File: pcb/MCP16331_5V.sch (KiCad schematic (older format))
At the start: 13 parts, among them U8 MCP16331T

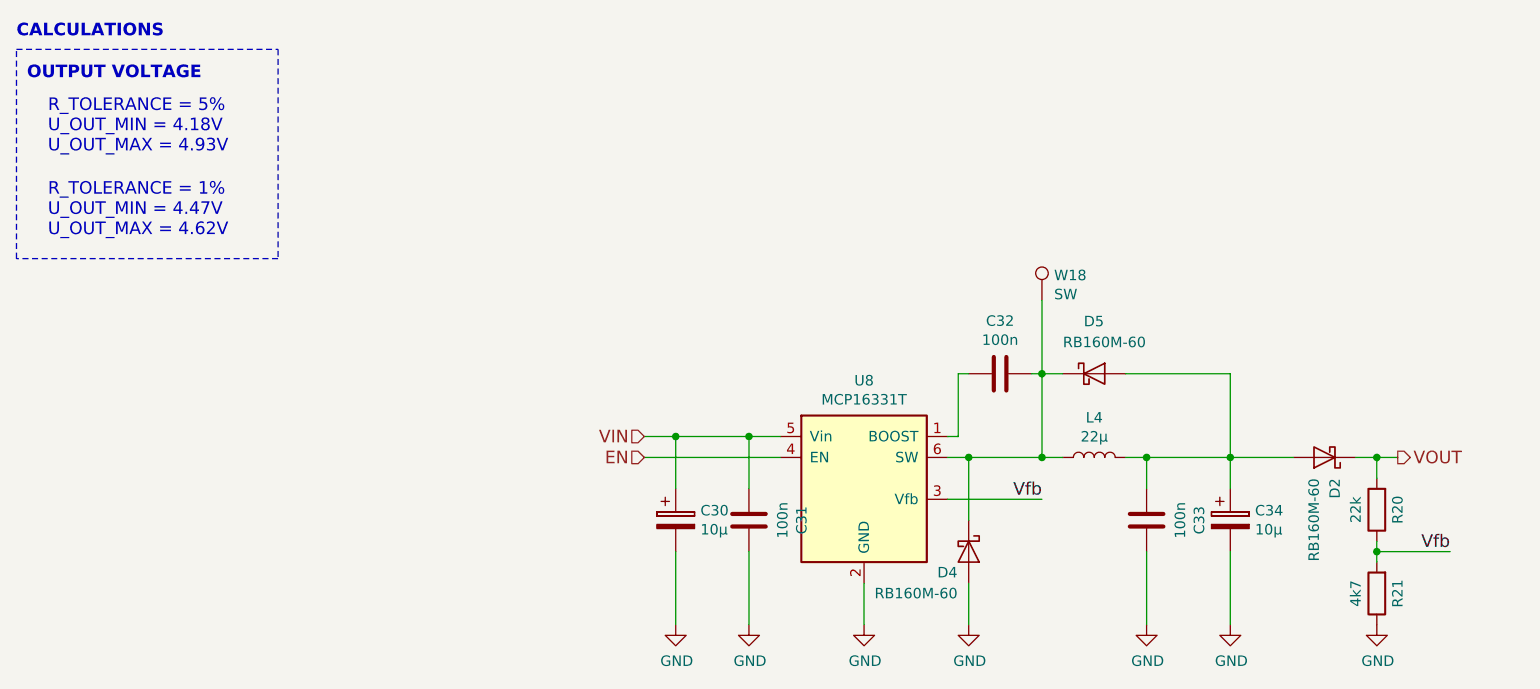
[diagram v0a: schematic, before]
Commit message: Fix schematic error described in #8
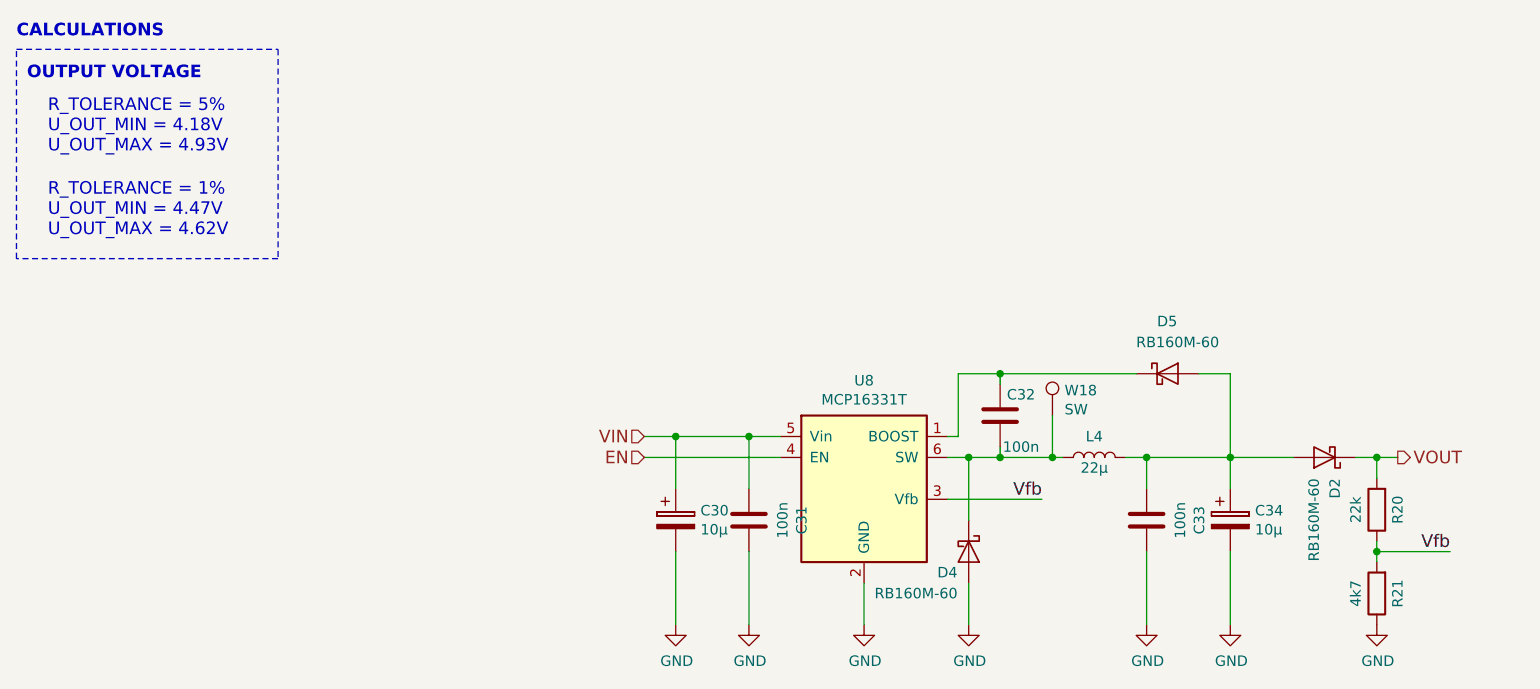
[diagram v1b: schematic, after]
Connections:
- net at C32.1, U8.1 (BOOST): now also D5.1 (K)
- net at C32.2, D4.1 (K), L4.1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: no longer D5.1 (K)
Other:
- moved on the sheet: C32, D5, W18
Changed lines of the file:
@@
 $EndComp
 $Comp
-L GND #PWR095
+L GND #PWR094
 U 1 1 580BA37A
 P 5300 4250
-F 0 "#PWR095" H 5300 4000 50  0001 C CNN
+F 0 "#PWR094" H 5300 4000 50  0001 C CNN
 F 1 "GND" H 5305 4077 50  0000 C CNN
 F 2 "" H 5300 4250 50  0000 C CNN
@@
 $EndComp
 $Comp
-L GND #PWR096
+L GND #PWR095
 U 1 1 580BA3A1
 P 4750 4250
-F 0 "#PWR096" H 4750 4000 50  0001 C CNN
+F 0 "#PWR095" H 4750 4000 50  0001 C CNN
 F 1 "GND" H 4755 4077 50  0000 C CNN
 F 2 "" H 4750 4250 50  0000 C CNN
@@
 $EndComp
 $Comp
-L GND #PWR097
+L GND #PWR096
 U 1 1 580BA3A7
 P 4400 4250
-F 0 "#PWR097" H 4400 4000 50  0001 C CNN
+F 0 "#PWR096" H 4400 4000 50  0001 C CNN
 F 1 "GND" H 4405 4077 50  0000 C CNN
 F 2 "" H 4400 4250 50  0000 C CNN
@@
 Wire Wire Line
 	4400 3900 4400 4250
-$Comp
-L C C32
-U 1 1 580BA3AF
-P 5950 3050
-F 0 "C32" V 6202 3050 50  0000 C CNN
-F 1 "100n" V 6111 3050 50  0000 C CNN
-F 2 "Capacitors_SMD:C_0603" H 5988 2900 50  0001 C CNN
-F 3 "" H 5950 3050 50  0000 C CNN
-F 4 "311-1343-1-ND" H 5950 3050 60  0001 C CNN "Digi-Key Part Number"
-F 5 "1" H 5950 3050 60  0001 C CNN "Digi-Key Minimum Quantity"
-	1    5950 3050
-	0    -1   -1   0
-$EndComp
-Wire Wire Line
-	5700 3450 6250 3450
-Wire Wire Line
-	6100 3050 6250 3050
-Wire Wire Line
-	6150 2700 6150 3450
-Connection ~ 6150 3450
+Wire Wire Line
+	5700 3450 5800 3450
+Wire Wire Line
+	5800 3450 5950 3450
+Wire Wire Line
+	5950 3450 6200 3450
+Wire Wire Line
+	6200 3450 6250 3450
 Wire Wire Line
 	5700 3350 5750 3350
 Wire Wire Line
-	5750 3350 5750 3050
-Wire Wire Line
-	5750 3050 5800 3050
+	5750 3050 5950 3050
+Wire Wire Line
+	5950 3050 6600 3050
 $Comp
 L CP C34
@@
 $EndComp
 $Comp
-L GND #PWR098
+L GND #PWR097
 U 1 1 580BA3CF
 P 6650 4250
-F 0 "#PWR098" H 6650 4000 50  0001 C CNN
+F 0 "#PWR097" H 6650 4000 50  0001 C CNN
 F 1 "GND" H 6655 4077 50  0000 C CNN
 F 2 "" H 6650 4250 50  0000 C CNN
@@
 $EndComp
 $Comp
-L GND #PWR099
+L GND #PWR098
 U 1 1 580BA3D5
 P 7050 4250
-F 0 "#PWR099" H 7050 4000 50  0001 C CNN
+F 0 "#PWR098" H 7050 4000 50  0001 C CNN
 F 1 "GND" H 7055 4077 50  0000 C CNN
 F 2 "" H 7050 4250 50  0000 C CNN
@@
 $EndComp
 $Comp
-L GND #PWR0100
+L GND #PWR099
 U 1 1 580BA3EB
 P 7750 4250
-F 0 "#PWR0100" H 7750 4000 50  0001 C CNN
+F 0 "#PWR099" H 7750 4000 50  0001 C CNN
 F 1 "GND" H 7755 4077 50  0000 C CNN
 F 2 "" H 7750 4250 50  0000 C CNN
@@
 Connection ~ 5800 3450
 $Comp
-L GND #PWR0101
+L GND #PWR0100
 U 1 1 580BA3FF
 P 5800 4250
-F 0 "#PWR0101" H 5800 4000 50  0001 C CNN
+F 0 "#PWR0100" H 5800 4000 50  0001 C CNN
 F 1 "GND" H 5805 4077 50  0000 C CNN
 F 2 "" H 5800 4250 50  0000 C CNN
@@
 L D_Schottky D5
 U 1 1 580BA407
-P 6400 3050
-F 0 "D5" H 6350 3300 50  0000 L CNN
-F 1 "RB160M-60" H 6250 3200 50  0000 L CNN
-F 2 "Diodes_SMD:SOD-123" H 6400 3050 50  0001 C CNN
-F 3 "" H 6400 3050 50  0000 C CNN
-	1    6400 3050
-	1    0    0    -1
-$EndComp
-Connection ~ 6150 3050
-Wire Wire Line
-	6550 3050 7050 3050
-Wire Wire Line
-	7050 3050 7050 3600
-Wire Wire Line
-	6550 3450 7350 3450
+P 6750 3050
+F 0 "D5" H 6700 3300 50  0000 L CNN
+F 1 "RB160M-60" H 6600 3200 50  0000 L CNN
+F 2 "Diodes_SMD:SOD-123" H 6750 3050 50  0001 C CNN
+F 3 "" H 6750 3050 50  0000 C CNN
+	1    6750 3050
+	1    0    0    -1
+$EndComp
+Wire Wire Line
+	6900 3050 7050 3050
+Wire Wire Line
+	7050 3050 7050 3450
+Wire Wire Line
+	7050 3450 7050 3600
+Wire Wire Line
+	6550 3450 6650 3450
+Wire Wire Line
+	6650 3450 7050 3450
+Wire Wire Line
+	7050 3450 7350 3450
 Wire Wire Line
 	6650 3450 6650 3600
@@
 VOUT
 Wire Wire Line
-	4250 3350 4900 3350
+	4250 3350 4400 3350
+Wire Wire Line
+	4400 3350 4750 3350
+Wire Wire Line
+	4750 3350 4900 3350
 Wire Wire Line
 	4400 3350 4400 3600
@@
 L TEST_1P W18
 U 1 1 5817A2DF
-P 6150 2700
-F 0 "W18" H 6208 2820 50  0000 L CNN
-F 1 "SW" H 6208 2729 50  0000 L CNN
-F 2 "Measurement_Points:Measurement_Point_Round-SMD-Pad_Small" H 6350 2700 50  0001 C CNN
-F 3 "" H 6350 2700 50  0000 C CNN
-	1    6150 2700
+P 6200 3250
+F 0 "W18" H 6258 3370 50  0000 L CNN
+F 1 "SW" H 6258 3279 50  0000 L CNN
+F 2 "Measurement_Points:Measurement_Point_Round-SMD-Pad_Small" H 6400 3250 50  0001 C CNN
+F 3 "" H 6400 3250 50  0000 C CNN
+	1    6200 3250
 	1    0    0    -1
 $EndComp
@@
 U 1 1 582ECCE6
 P 6400 3450
-F 0 "L4" V 6590 3450 50  0000 C CNN
-F 1 "22µ" V 6499 3450 50  0000 C CNN
+F 0 "L4" V 6500 3450 50  0000 C CNN
+F 1 "22µ" V 6350 3450 50  0000 C CNN
 F 2 "Inductors_local:Inductor_Würth_WE-PD2_4532" V 6498 3450 50  0001 C CNN
 F 3 "http://katalog.we-online.de/pbs/datasheet/744773122.pdf" V 6498 3450 50  0001 C CNN
@@
 $EndComp
 Wire Wire Line
-	7850 3450 7650 3450
+	7650 3450 7750 3450
+Wire Wire Line
+	7750 3450 7850 3450
 Wire Wire Line
 	7750 3550 7750 3450
 Connection ~ 7750 3450
 Wire Wire Line
-	7750 3850 7750 3950
+	7750 3850 7750 3900
+Wire Wire Line
+	7750 3900 7750 3950
 Wire Wire Line
 	7750 3900 8100 3900
@@
 Wire Wire Line
 	4750 3600 4750 3350
+$Comp
+L C C32
+U 1 1 580BA3AF
+P 5950 3250
+F 0 "C32" H 6050 3350 50  0000 C CNN
+F 1 "100n" H 6050 3100 50  0000 C CNN
+F 2 "Capacitors_SMD:C_0603" H 5988 3100 50  0001 C CNN
+F 3 "" H 5950 3250 50  0000 C CNN
+F 4 "311-1343-1-ND" H 5950 3250 60  0001 C CNN "Digi-Key Part Number"
+F 5 "1" H 5950 3250 60  0001 C CNN "Digi-Key Minimum Quantity"
+	1    5950 3250
+	1    0    0    -1
+$EndComp
+Wire Wire Line
+	5750 3350 5750 3050
+Wire Wire Line
+	5950 3450 5950 3400
+Connection ~ 5950 3450
+Wire Wire Line
+	5950 3100 5950 3050
+Connection ~ 5950 3050
+Wire Wire Line
+	6200 3250 6200 3450
+Connection ~ 6200 3450
 $EndSCHEMATC

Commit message: Update schematic
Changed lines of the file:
@@
 	4400 3900 4400 4250
 Wire Wire Line
-	5700 3450 5800 3450
-Wire Wire Line
-	5800 3450 5950 3450
-Wire Wire Line
-	5950 3450 6200 3450
-Wire Wire Line
-	6200 3450 6250 3450
+	5700 3450 6250 3450
 Wire Wire Line
 	5700 3350 5750 3350
 Wire Wire Line
-	5750 3050 5950 3050
-Wire Wire Line
-	5950 3050 6600 3050
+	5750 3050 6600 3050
 $Comp
 L CP C34
@@
 	6900 3050 7050 3050
 Wire Wire Line
-	7050 3050 7050 3450
-Wire Wire Line
-	7050 3450 7050 3600
-Wire Wire Line
-	6550 3450 6650 3450
-Wire Wire Line
-	6650 3450 7050 3450
-Wire Wire Line
-	7050 3450 7350 3450
+	7050 3050 7050 3600
+Wire Wire Line
+	6550 3450 7350 3450
 Wire Wire Line
 	6650 3450 6650 3600
@@
 VOUT
 Wire Wire Line
-	4250 3350 4400 3350
-Wire Wire Line
-	4400 3350 4750 3350
-Wire Wire Line
-	4750 3350 4900 3350
+	4250 3350 4900 3350
 Wire Wire Line
 	4400 3350 4400 3600
@@
 $EndComp
 Wire Wire Line
-	7650 3450 7750 3450
-Wire Wire Line
-	7750 3450 7850 3450
+	7650 3450 7850 3450
 Wire Wire Line
 	7750 3550 7750 3450
 Connection ~ 7750 3450
 Wire Wire Line
-	7750 3850 7750 3900
-Wire Wire Line
-	7750 3900 7750 3950
+	7750 3850 7750 3950
 Wire Wire Line
 	7750 3900 8100 3900

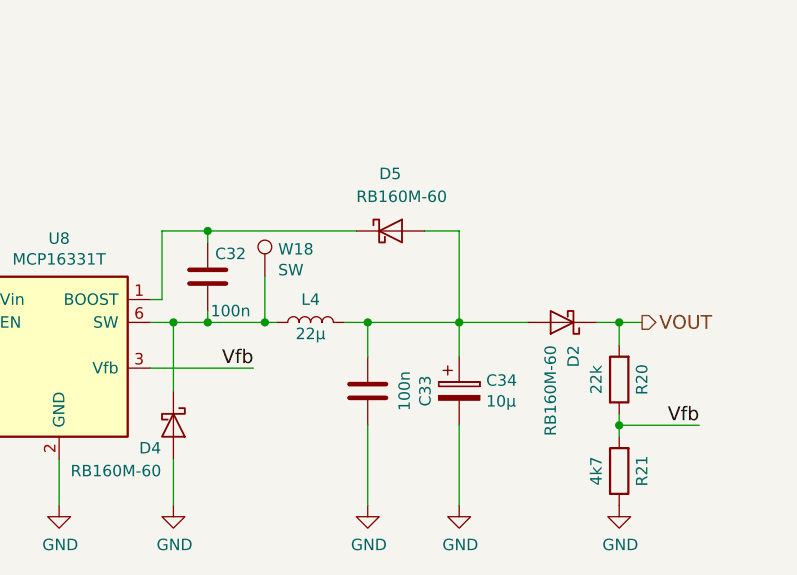
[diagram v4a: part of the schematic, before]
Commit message: Some changes to the step down converter, Fix #8
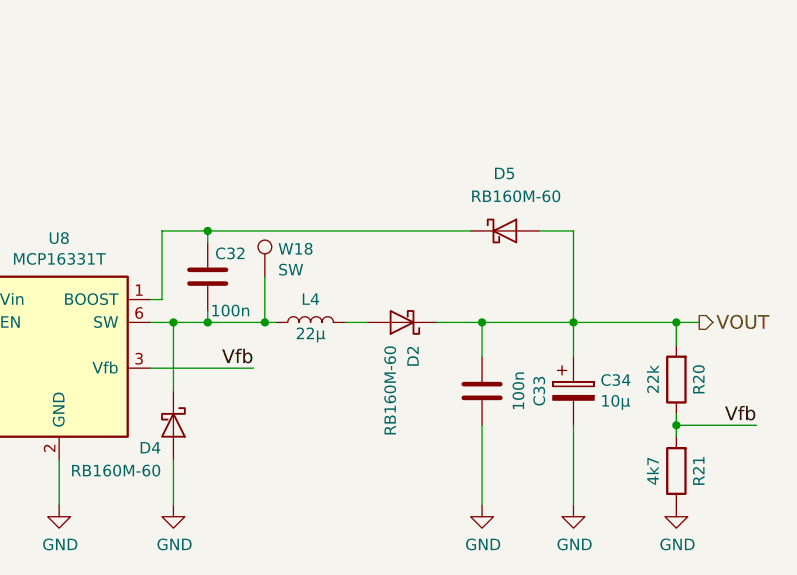
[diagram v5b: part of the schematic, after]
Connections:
- net VOUT: now also C33.1, C34.1, D5.2 (A)
- new net: D2.2 (A), L4.2
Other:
- moved on the sheet: C33, C34, D2, D5, R20, R21
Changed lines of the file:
@@
 LIBS:ftdi
 LIBS:gennum
-LIBS:graphic
 LIBS:hc11
 LIBS:intel
@@
 LIBS:microchip_pic16mcu
 LIBS:microchip_pic18mcu
-LIBS:microchip_pic32mcu
 LIBS:microcontrollers
 LIBS:motor_drivers
@@
 	5700 3350 5750 3350
 Wire Wire Line
-	5750 3050 6600 3050
+	5750 3050 7100 3050
 $Comp
 L CP C34
 U 1 1 580BA3C4
-P 7050 3750
-F 0 "C34" H 7168 3796 50  0000 L CNN
-F 1 "10µ" H 7168 3705 50  0000 L CNN
-F 2 "Capacitors_SMD_local:c_elec_6.6x5.8" H 7088 3600 50  0001 C CNN
-F 3 "http://www.chemi-con.co.jp/cgi-bin/CAT_DB/SEARCH/cat_db_al.cgi?e=e&j=p&pdfname=hxb" H 7050 3750 50  0001 C CNN
-F 4 "565-4191-1-ND" H 7050 3750 60  0001 C CNN "Digi-Key Part Number"
-F 5 "1" H 7050 3750 60  0001 C CNN "Digi-Key Minimum Quantity"
-	1    7050 3750
+P 7550 3750
+F 0 "C34" H 7668 3796 50  0000 L CNN
+F 1 "10µ" H 7668 3705 50  0000 L CNN
+F 2 "Capacitors_SMD_local:c_elec_6.6x5.8" H 7588 3600 50  0001 C CNN
+F 3 "http://www.chemi-con.co.jp/cgi-bin/CAT_DB/SEARCH/cat_db_al.cgi?e=e&j=p&pdfname=hxb" H 7550 3750 50  0001 C CNN
+F 4 "565-4191-1-ND" H 7550 3750 60  0001 C CNN "Digi-Key Part Number"
+F 5 "1" H 7550 3750 60  0001 C CNN "Digi-Key Minimum Quantity"
+	1    7550 3750
 	1    0    0    -1
 $EndComp
@@
 L GND #PWR096
 U 1 1 580BA3CF
-P 6650 4250
-F 0 "#PWR096" H 6650 4000 50  0001 C CNN
-F 1 "GND" H 6655 4077 50  0000 C CNN
-F 2 "" H 6650 4250 50  0000 C CNN
-F 3 "" H 6650 4250 50  0000 C CNN
-	1    6650 4250
+P 7150 4250
+F 0 "#PWR096" H 7150 4000 50  0001 C CNN
+F 1 "GND" H 7155 4077 50  0000 C CNN
+F 2 "" H 7150 4250 50  0000 C CNN
+F 3 "" H 7150 4250 50  0000 C CNN
+	1    7150 4250
 	1    0    0    -1
 $EndComp
@@
 L GND #PWR097
 U 1 1 580BA3D5
-P 7050 4250
-F 0 "#PWR097" H 7050 4000 50  0001 C CNN
-F 1 "GND" H 7055 4077 50  0000 C CNN
-F 2 "" H 7050 4250 50  0000 C CNN
-F 3 "" H 7050 4250 50  0000 C CNN
-	1    7050 4250
-	1    0    0    -1
-$EndComp
-Wire Wire Line
-	6650 3900 6650 4250
-Wire Wire Line
-	7050 3900 7050 4250
+P 7550 4250
+F 0 "#PWR097" H 7550 4000 50  0001 C CNN
+F 1 "GND" H 7555 4077 50  0000 C CNN
+F 2 "" H 7550 4250 50  0000 C CNN
+F 3 "" H 7550 4250 50  0000 C CNN
+	1    7550 4250
+	1    0    0    -1
+$EndComp
+Wire Wire Line
+	7150 3900 7150 4250
+Wire Wire Line
+	7550 3900 7550 4250
 $Comp
 L R R20
 U 1 1 580BA3DD
-P 7750 3700
-F 0 "R20" V 7650 3700 50  0000 C CNN
-F 1 "22k" V 7850 3700 50  0000 C CNN
-F 2 "Resistors_SMD:R_0603" V 7680 3700 50  0001 C CNN
-F 3 "" H 7750 3700 50  0000 C CNN
-F 4 "311-22.0KHRCT-ND" H 7750 3700 60  0001 C CNN "Digi-Key Part Number"
-F 5 "1" H 7750 3700 60  0001 C CNN "Digi-Key Minimum Quantity"
-	1    7750 3700
+P 8000 3700
+F 0 "R20" V 7900 3700 50  0000 C CNN
+F 1 "22k" V 8100 3700 50  0000 C CNN
+F 2 "Resistors_SMD:R_0603" V 7930 3700 50  0001 C CNN
+F 3 "" H 8000 3700 50  0000 C CNN
+F 4 "311-22.0KHRCT-ND" H 8000 3700 60  0001 C CNN "Digi-Key Part Number"
+F 5 "1" H 8000 3700 60  0001 C CNN "Digi-Key Minimum Quantity"
+	1    8000 3700
 	-1   0    0    1
 $EndComp
@@
 L R R21
 U 1 1 580BA3E4
-P 7750 4100
-F 0 "R21" V 7650 4100 50  0000 C CNN
-F 1 "4k7" V 7850 4100 50  0000 C CNN
-F 2 "Resistors_SMD:R_0603" V 7680 4100 50  0001 C CNN
-F 3 "" H 7750 4100 50  0000 C CNN
-F 4 "311-4.70KHRCT-ND" H 7750 4100 60  0001 C CNN "Digi-Key Part Number"
-F 5 "1" H 7750 4100 60  0001 C CNN "Digi-Key Minimum Quantity"
-	1    7750 4100
+P 8000 4100
+F 0 "R21" V 7900 4100 50  0000 C CNN
+F 1 "4k7" V 8100 4100 50  0000 C CNN
+F 2 "Resistors_SMD:R_0603" V 7930 4100 50  0001 C CNN
+F 3 "" H 8000 4100 50  0000 C CNN
+F 4 "311-4.70KHRCT-ND" H 8000 4100 60  0001 C CNN "Digi-Key Part Number"
+F 5 "1" H 8000 4100 60  0001 C CNN "Digi-Key Minimum Quantity"
+	1    8000 4100
 	-1   0    0    1
 $EndComp
@@
 L GND #PWR098
 U 1 1 580BA3EB
-P 7750 4250
-F 0 "#PWR098" H 7750 4000 50  0001 C CNN
-F 1 "GND" H 7755 4077 50  0000 C CNN
-F 2 "" H 7750 4250 50  0000 C CNN
-F 3 "" H 7750 4250 50  0000 C CNN
-	1    7750 4250
+P 8000 4250
+F 0 "#PWR098" H 8000 4000 50  0001 C CNN
+F 1 "GND" H 8005 4077 50  0000 C CNN
+F 2 "" H 8000 4250 50  0000 C CNN
+F 3 "" H 8000 4250 50  0000 C CNN
+	1    8000 4250
 	1    0    0    -1
 $EndComp
@@
 L D_Schottky D5
 U 1 1 580BA407
-P 6750 3050
-F 0 "D5" H 6700 3300 50  0000 L CNN
-F 1 "RB160M-60" H 6600 3200 50  0000 L CNN
-F 2 "Diodes_SMD:SOD-123" H 6750 3050 50  0001 C CNN
-F 3 "" H 6750 3050 50  0000 C CNN
-	1    6750 3050
-	1    0    0    -1
-$EndComp
-Wire Wire Line
-	6900 3050 7050 3050
-Wire Wire Line
-	7050 3050 7050 3600
-Wire Wire Line
-	6550 3450 7350 3450
-Wire Wire Line
-	6650 3450 6650 3600
-Connection ~ 7050 3450
-Connection ~ 6650 3450
-Text HLabel 7850 3450 2    60   Output ~ 0
+P 7250 3050
+F 0 "D5" H 7200 3300 50  0000 L CNN
+F 1 "RB160M-60" H 7100 3200 50  0000 L CNN
+F 2 "Diodes_SMD:SOD-123" H 7250 3050 50  0001 C CNN
+F 3 "" H 7250 3050 50  0000 C CNN
+	1    7250 3050
+	1    0    0    -1
+$EndComp
+Wire Wire Line
+	7400 3050 7550 3050
+Wire Wire Line
+	7550 3050 7550 3600
+Wire Wire Line
+	6950 3450 8100 3450
+Wire Wire Line
+	7150 3450 7150 3600
+Connection ~ 7550 3450
+Connection ~ 7150 3450
+Text HLabel 8100 3450 2    60   Output ~ 0
 VOUT
 Wire Wire Line
@@
 L D_Schottky D2
 U 1 1 583B1A52
-P 7500 3450
-F 0 "D2" V 7450 3550 50  0000 L CNN
-F 1 "RB160M-60" V 7550 3550 50  0000 L CNN
-F 2 "Diodes_SMD:SOD-123" H 7500 3450 50  0001 C CNN
-F 3 "http://rohmfs.rohm.com/en/products/databook/datasheet/discrete/diode/schottky_barrier/rb160m-60.pdf" H 7500 3450 50  0001 C CNN
-F 4 "RB160M-90DKR-ND" H 7500 3450 60  0001 C CNN "Digi-Key Part Number"
-F 5 "1" H 7500 3450 60  0001 C CNN "Digi-Key Minimum Quantity"
-	1    7500 3450
+P 6800 3450
+F 0 "D2" V 6750 3550 50  0000 L CNN
+F 1 "RB160M-60" V 6850 3550 50  0000 L CNN
+F 2 "Diodes_SMD:SOD-123" H 6800 3450 50  0001 C CNN
+F 3 "http://rohmfs.rohm.com/en/products/databook/datasheet/discrete/diode/schottky_barrier/rb160m-60.pdf" H 6800 3450 50  0001 C CNN
+F 4 "RB160M-90DKR-ND" H 6800 3450 60  0001 C CNN "Digi-Key Part Number"
+F 5 "1" H 6800 3450 60  0001 C CNN "Digi-Key Minimum Quantity"
+	1    6800 3450
 	-1   0    0    1
 $EndComp
 Wire Wire Line
-	7650 3450 7850 3450
-Wire Wire Line
-	7750 3550 7750 3450
-Connection ~ 7750 3450
-Wire Wire Line
-	7750 3850 7750 3950
-Wire Wire Line
-	7750 3900 8100 3900
-Connection ~ 7750 3900
+	8000 3550 8000 3450
+Connection ~ 8000 3450
+Wire Wire Line
+	8000 3850 8000 3950
+Wire Wire Line
+	8000 3900 8350 3900
+Connection ~ 8000 3900
 Text Label 6150 3650 2    60   ~ 0
 Vfb
-Text Label 8100 3900 2    60   ~ 0
+Text Label 8350 3900 2    60   ~ 0
 Vfb
 Wire Wire Line
@@
 L C C33
 U 1 1 583CD4BA
-P 6650 3750
-F 0 "C33" V 6902 3750 50  0000 C CNN
-F 1 "100n" V 6811 3750 50  0000 C CNN
-F 2 "Capacitors_SMD:C_0603" H 6688 3600 50  0001 C CNN
-F 3 "" H 6650 3750 50  0000 C CNN
-F 4 "311-1343-1-ND" H 6650 3750 60  0001 C CNN "Digi-Key Part Number"
-F 5 "1" H 6650 3750 60  0001 C CNN "Digi-Key Minimum Quantity"
-	1    6650 3750
+P 7150 3750
+F 0 "C33" V 7402 3750 50  0000 C CNN
+F 1 "100n" V 7311 3750 50  0000 C CNN
+F 2 "Capacitors_SMD:C_0603" H 7188 3600 50  0001 C CNN
+F 3 "" H 7150 3750 50  0000 C CNN
+F 4 "311-1343-1-ND" H 7150 3750 60  0001 C CNN "Digi-Key Part Number"
+F 5 "1" H 7150 3750 60  0001 C CNN "Digi-Key Minimum Quantity"
+	1    7150 3750
 	1    0    0    -1
 $EndComp
@@
 	6200 3250 6200 3450
 Connection ~ 6200 3450
+Wire Wire Line
+	6650 3450 6550 3450
 $EndSCHEMATC
